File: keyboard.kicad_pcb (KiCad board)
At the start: 2 copper layers, 24 parts, among them SW1 SW_Push, SW10 SW_Push, SW11 SW_Push, SW12 RotaryEncoder_Switch, SW2 SW_Push, SW3 SW_Push, SW4 SW_Push, SW5 SW_Push, SW6 SW_Push, SW7 SW_Push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

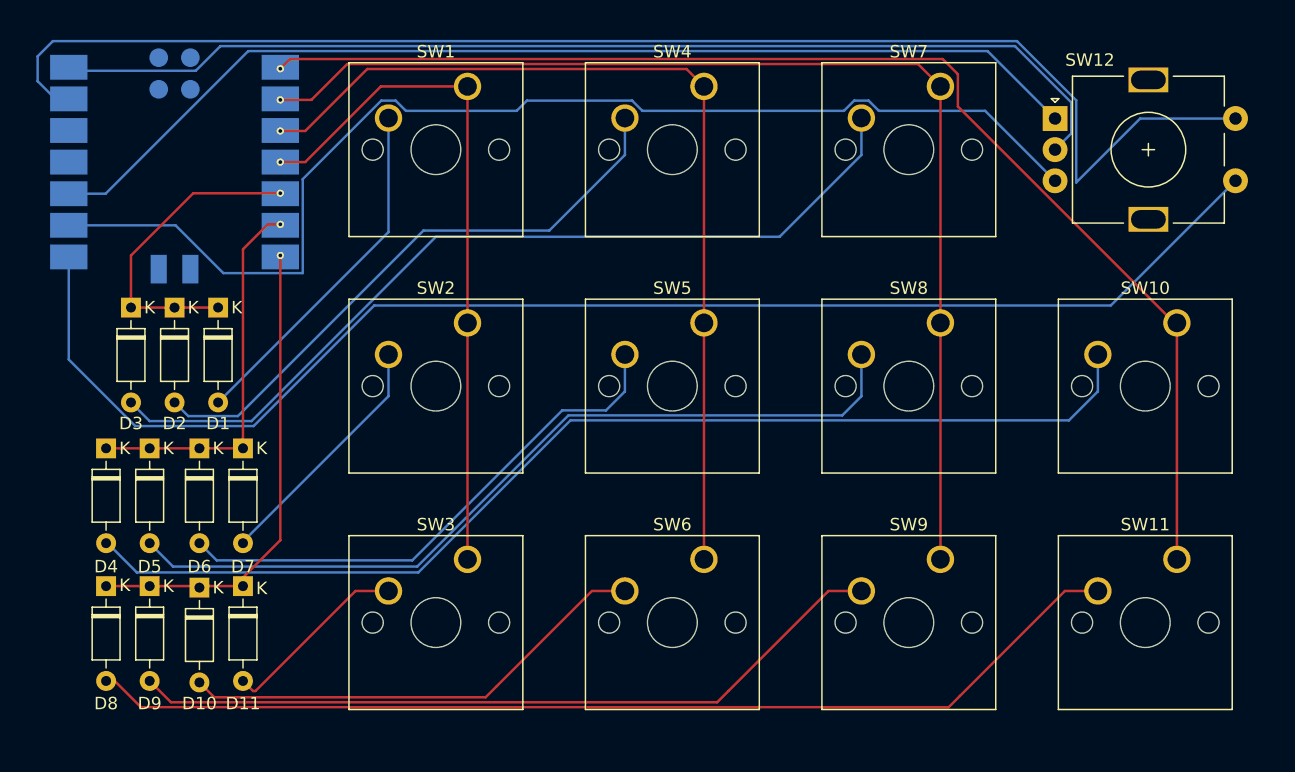
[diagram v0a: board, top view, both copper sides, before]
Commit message: rewired the rotary encoder into the matrix
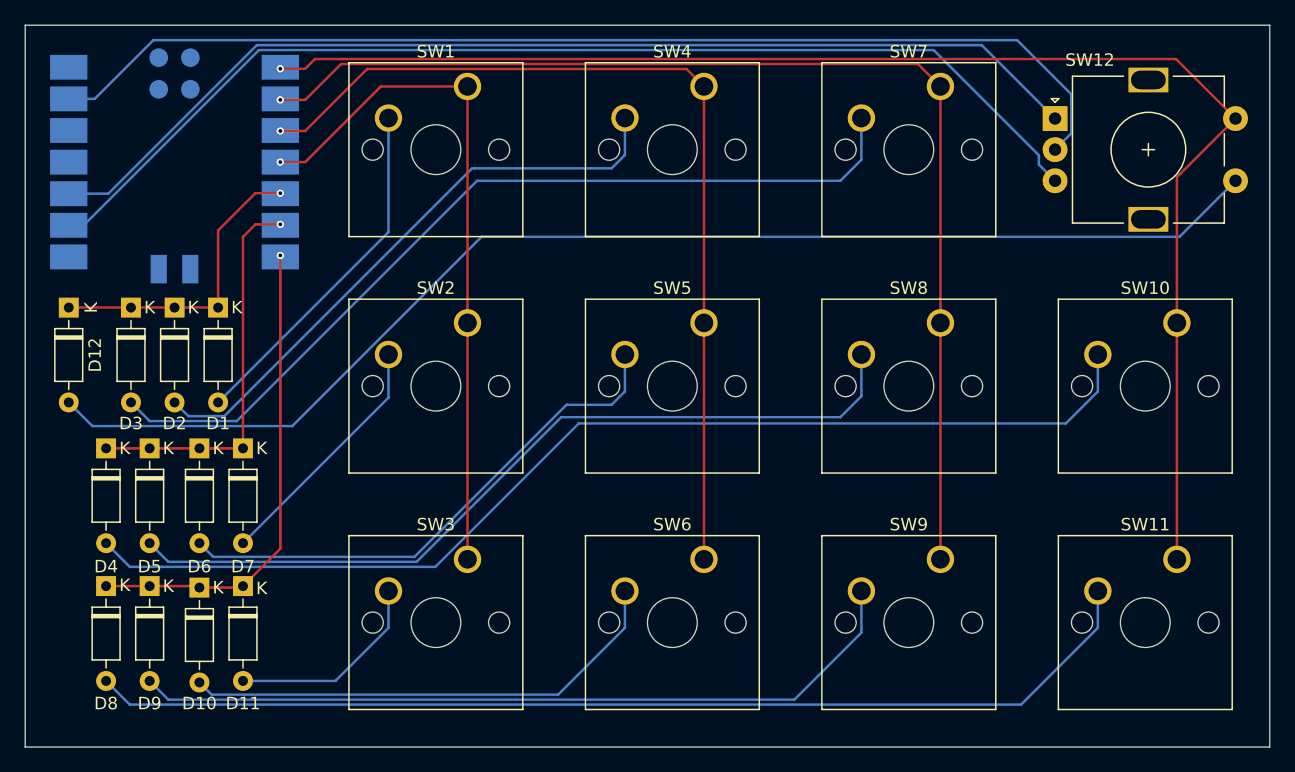
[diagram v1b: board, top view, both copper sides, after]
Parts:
- added D12: 1N4148, Diode_THT:D_DO-35_SOD27_P7.62mm_Horizontal, F.Cu at (48.5, 95.7)
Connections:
- SW12 pad C: Net-(SW12-PadC) -> GND
- SW12 pad S1: Net-(U1-PB09_A7_D7_RX) -> Net-(D12-A)
- SW12 pad S2: GND -> Net-(U1-PA02_A0_D0)
- U1 pad 14: Net-(SW12-PadC) -> unconnected-(U1-5V-Pad14)
- U1 pad 8: Net-(U1-PB09_A7_D7_RX) -> unconnected-(U1-PB09_A7_D7_RX-Pad8)
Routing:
- net Net-(U1-PB09_A7_D7_RX): track 112.4 -> 0.00 mm
- net Net-(D12-A): track 0.00 -> 102.7 mm
- net Net-(SW12-PadC): track 87.7 -> 0.00 mm
- net GND: track 112.5 -> 89.3 mm
- net Net-(U1-PA02_A0_D0): track 101.7 -> 116.4 mm
- net Net-(U1-PA7_A8_D8_SCK): track 95.0 -> 89.9 mm
- net Net-(D9-A): track 61.6 -> 63.4 mm
- net Net-(D10-A): track 38.2 -> 39.8 mm
- net Net-(D8-A): track 84.4 -> 86.0 mm
- net Net-(D1-K): track 26.0 -> 24.4 mm
- net Net-(D11-A): track 15.4 -> 16.4 mm
- net Net-(D4-K): track 30.7 -> 31.4 mm
- net Net-(D6-A): track 43.8 -> 43.1 mm
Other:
- board outline added: 100 x 58 mm

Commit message: changed to a through hole microprocessor
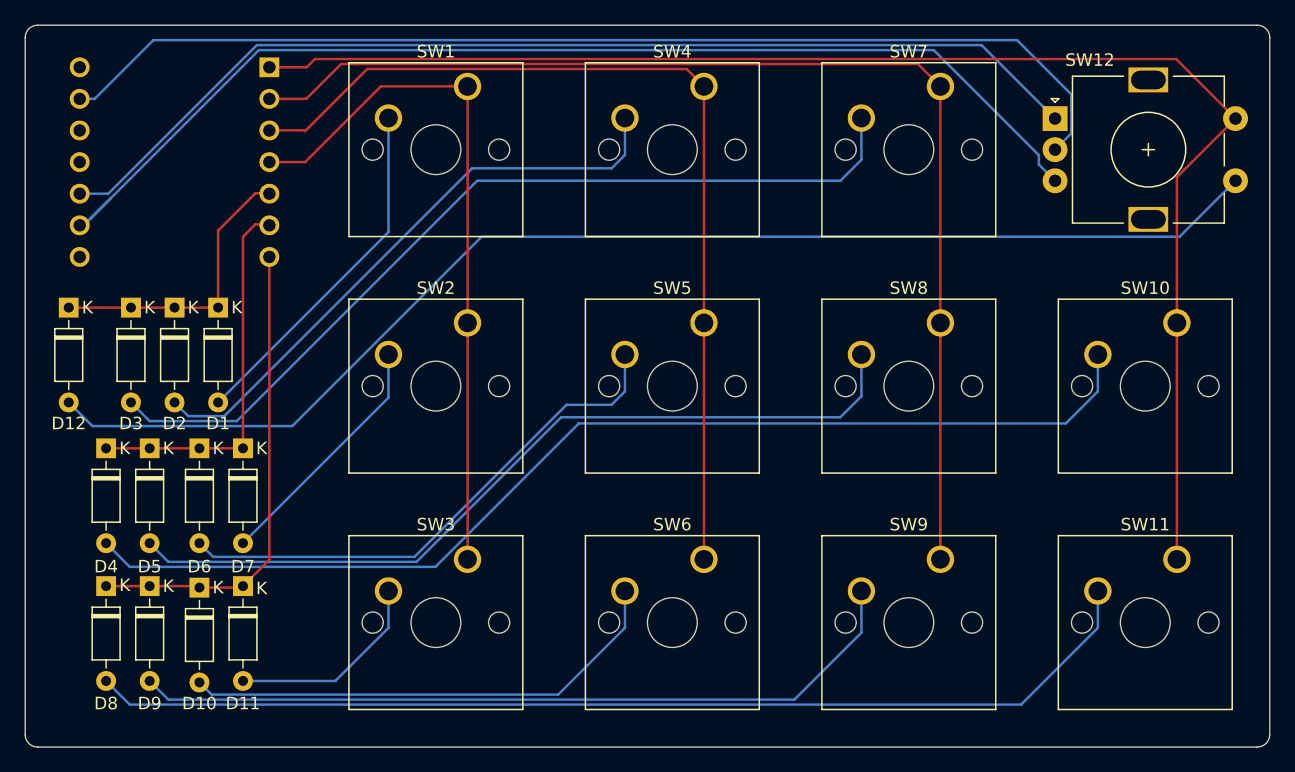
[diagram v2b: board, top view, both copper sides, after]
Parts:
- U1: footprint Seeed Studio XIAO Series Library:XIAO-SAMD21-RP2040-14P-2.54-21X17.8MM (Seeeduino XIAO) -> XIAO_PCB:MOUDLE14P-2.54-21X17.8MM
- turned U1 to 90 degrees
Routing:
- net Net-(U1-PA7_A8_D8_SCK): track 89.9 -> 92.1 mm
- net Net-(U1-PA10_A2_D2): track 74.7 -> 75.6 mm, vias 1 -> 0
- net Net-(U1-PA5_A9_D9_MISO): track 86.6 -> 85.8 mm
- net GND: track 89.3 -> 88.4 mm
- net Net-(U1-PA11_A3_D3): track 55.6 -> 56.4 mm, vias 1 -> 0
- net Net-(D1-K): track 24.4 -> 23.6 mm, vias 1 -> 0
- net Net-(U1-PA4_A1_D1): track 93.0 -> 93.8 mm, vias 1 -> 0
- net Net-(D4-K): track 31.4 -> 30.6 mm, vias 1 -> 0
- net Net-(U1-PA02_A0_D0): track 116.4 -> 117.3 mm, vias 1 -> 0
- net Net-(D10-K): track 38.9 -> 38.4 mm, vias 1 -> 0
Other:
- outline, holes or cut-outs redrawn
